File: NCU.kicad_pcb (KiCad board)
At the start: 2 copper layers, 88.5 x 126 mm, 126 parts, among them IC1 LMR51460SQDRRRQ1, IC2 TPS628101HQWRWYRQ1, J1 RJ45, J2 USB_B, J3 Micro_SD_Card, J4 6437288-4, J5 6437288-4, J6 Bus_PCI_Express_Mini, Q1 CSD25483F4, Q2 CSD25483F4, U1 STM32H745ZITx, U3 SN65HVD230, U4 SN65HVD230, U5 XL1509-3.3, U6 ESP32-C3-WROOM-02, U7 AP2112K-1.8, U8 LAN8742A

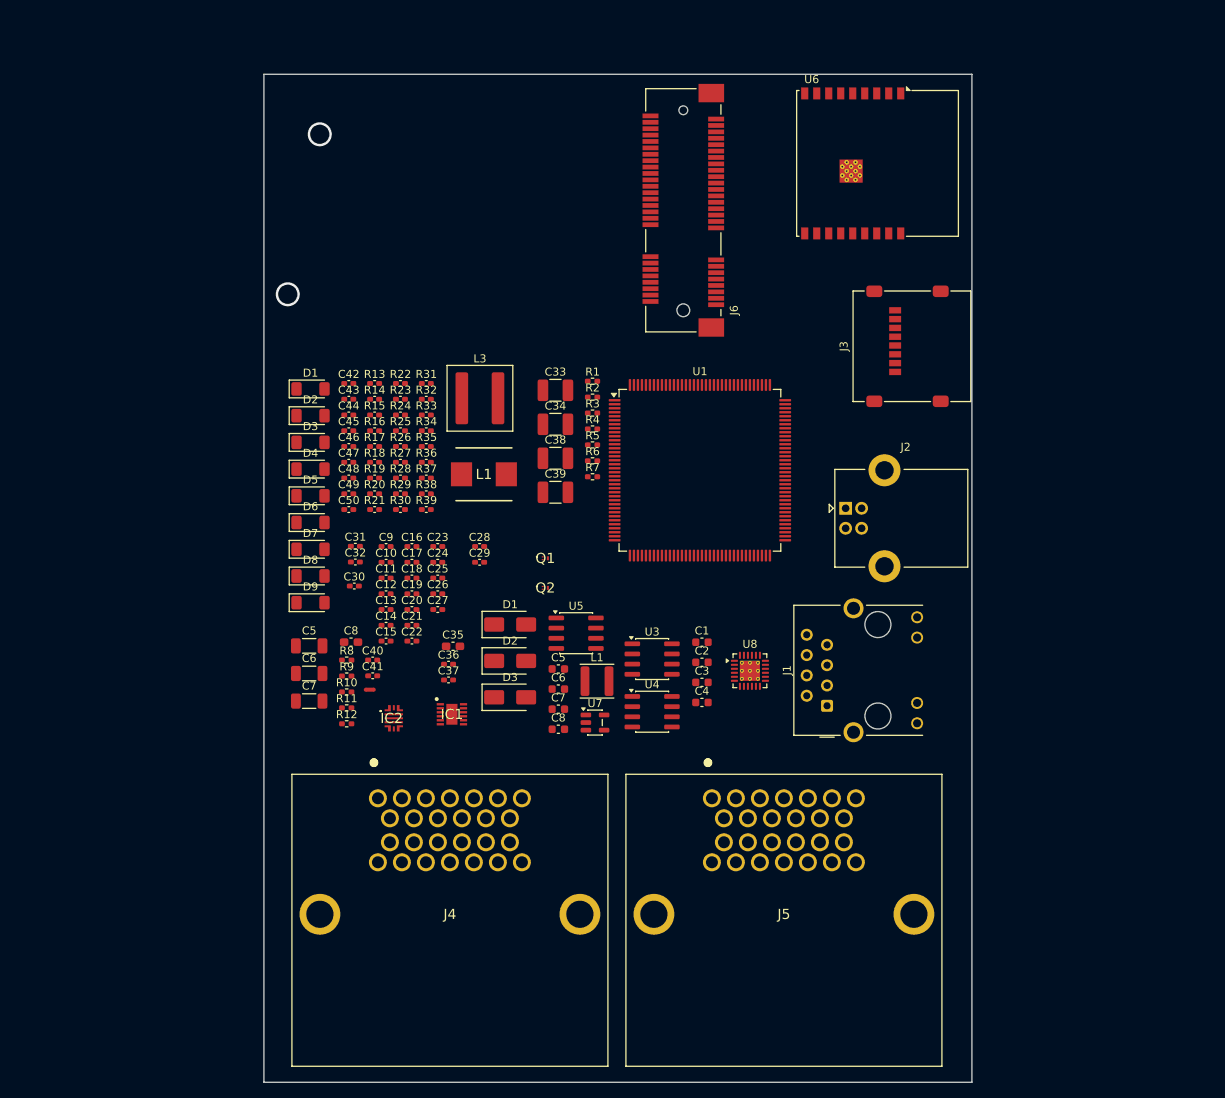
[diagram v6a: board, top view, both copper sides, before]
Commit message: redid annotations, added test point
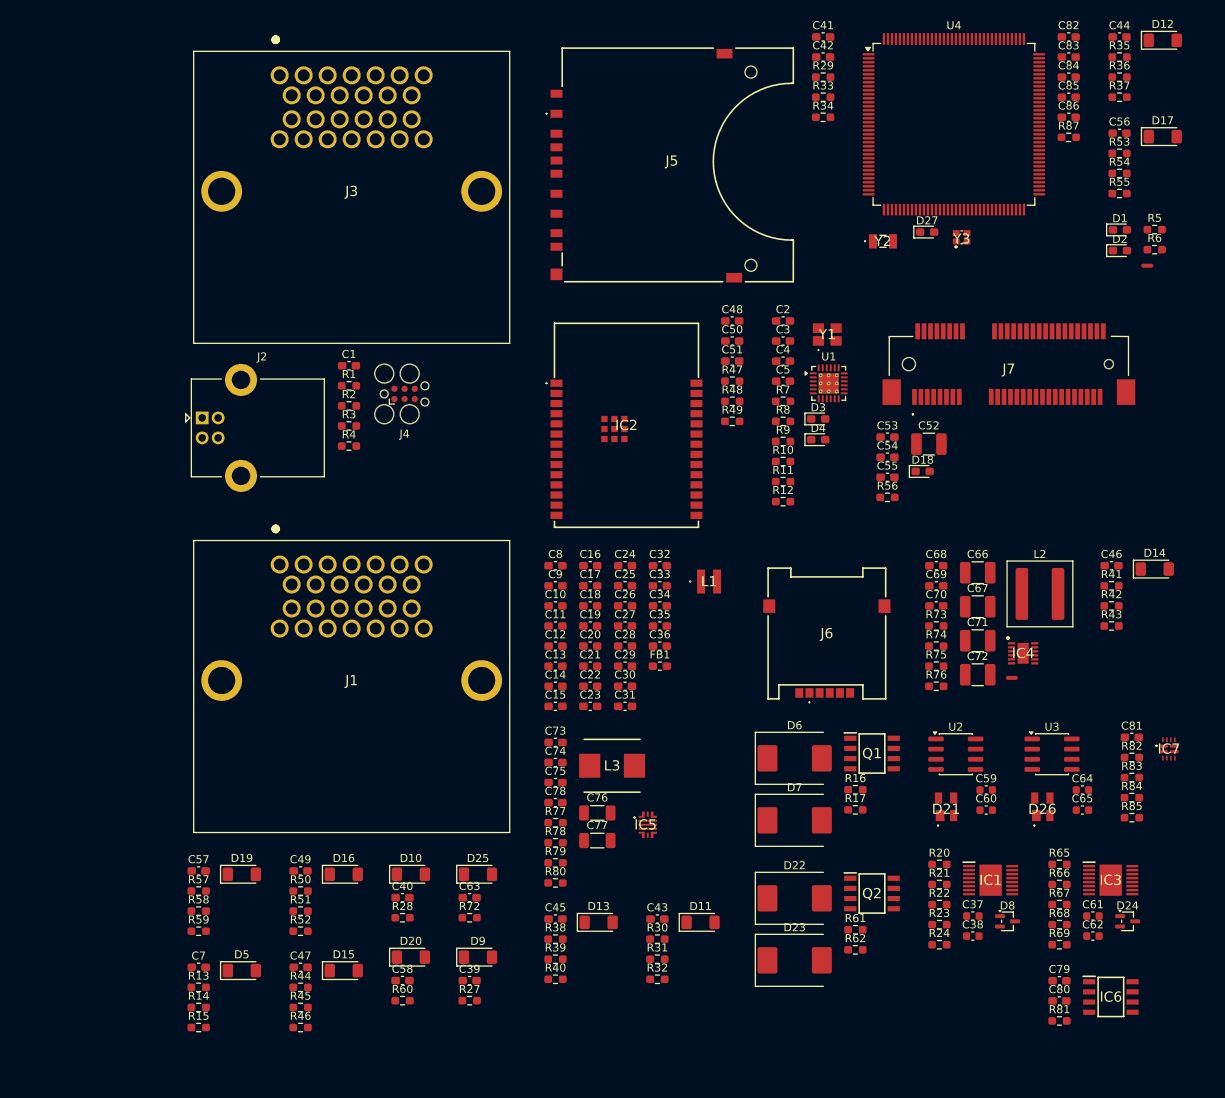
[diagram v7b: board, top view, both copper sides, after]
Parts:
- removed the C5 at (97.3, 116.8)
- removed the C5 at (66.2, 114.0)
- removed C6: 22uF, Inductor_SMD:L_1206_3216Metric_Pad1.22x1.90mm_HandSolder
- removed C6: 470uF, Capacitor_SMD:C_0603_1608Metric
- removed the C7 at (97.3, 121.9)
- removed the C7 at (66.2, 120.8)
- removed the C8 at (71.4, 113.5)
- removed the C8 at (97.3, 124.4)
- removed the D1 at (91.3, 111.3)
- removed the D1 at (66.3, 81.8)
- removed the D2 at (66.3, 85.2)
- removed the D2 at (91.3, 115.8)
- removed the D3 at (91.3, 120.4)
- removed the D3 at (66.3, 88.5)
- removed the L1 at (88.0, 92.5)
- removed the L1 at (102.2, 118.4)
- removed R18: 100, Capacitor_SMD:C_0402_1005Metric_Pad0.74x0.62mm_HandSolder
- removed R19, R25: 10k, Capacitor_SMD:C_0402_1005Metric_Pad0.74x0.62mm_HandSolder
- removed R26: 20k, Capacitor_SMD:C_0402_1005Metric_Pad0.74x0.62mm_HandSolder
- removed U5: XL1509-3.3, Package_SO:SOIC-8_3.9x4.9mm_P1.27mm
- removed U6: ESP32-C3-WROOM-02, RF_Module:ESP32-C3-WROOM-02
- removed U7: AP2112K-1.8, Package_TO_SOT_SMD:SOT-23-5
- removed U8: LAN8742A, Package_DFN_QFN:VQFN-24-1EP_4x4mm_P0.5mm_EP2.5x2.5mm_ThermalVias
- added C5: 10pF, Capacitor_SMD:C_0603_1608Metric_Pad1.08x0.95mm_HandSolder, F.Cu at (125.4, 80.9)
- added C51: 100n, Capacitor_SMD:C_0603_1608Metric_Pad1.08x0.95mm_HandSolder, F.Cu at (119.1, 78.4)
- added C52: 100uF, Capacitor_SMD:C_1210_3225Metric_Pad1.33x2.70mm_HandSolder, F.Cu at (143.6, 88.7)
- added C53: 10uF, Capacitor_SMD:C_0603_1608Metric_Pad1.08x0.95mm_HandSolder, F.Cu at (138.5, 87.9)
- added C54: 100nF, Capacitor_SMD:C_0603_1608Metric_Pad1.08x0.95mm_HandSolder, F.Cu at (138.5, 90.4)
- added C55: 100nF, Capacitor_SMD:C_0603_1608Metric_Pad1.08x0.95mm_HandSolder, F.Cu at (138.5, 92.9)
- added C56: 100nF, Capacitor_SMD:C_0603_1608Metric_Pad1.08x0.95mm_HandSolder, F.Cu at (167.5, 49.9)
- added C57: 100nF, Capacitor_SMD:C_0603_1608Metric_Pad1.08x0.95mm_HandSolder, F.Cu at (52.4, 142.1)
- added C58: 100nF, Capacitor_SMD:C_0603_1608Metric_Pad1.08x0.95mm_HandSolder, F.Cu at (77.8, 155.8)
- added C59: 1u, Capacitor_SMD:C_0603_1608Metric, F.Cu at (150.8, 132.0)
- added C60: 100n, Capacitor_SMD:C_0603_1608Metric, F.Cu at (150.8, 134.5)
- added C61: 10u, Capacitor_SMD:C_0603_1608Metric, F.Cu at (164.1, 147.7)
- added C62: 100n, Capacitor_SMD:C_0603_1608Metric, F.Cu at (164.1, 150.2)
- added C63: 100nF, Capacitor_SMD:C_0603_1608Metric_Pad1.08x0.95mm_HandSolder, F.Cu at (86.2, 145.4)
- added C64: 1u, Capacitor_SMD:C_0603_1608Metric, F.Cu at (162.8, 132.0)
- added C65: 100n, Capacitor_SMD:C_0603_1608Metric, F.Cu at (162.8, 134.5)
- added C66: 4.7uF, Capacitor_SMD:C_1210_3225Metric_Pad1.33x2.70mm_HandSolder, F.Cu at (149.7, 104.8)
- added C67: 4.7uF, Capacitor_SMD:C_1210_3225Metric_Pad1.33x2.70mm_HandSolder, F.Cu at (149.7, 109.1)
- added C68: 0.1uF, Capacitor_SMD:C_0603_1608Metric_Pad1.08x0.95mm_HandSolder, F.Cu at (144.6, 103.9)
- added C69: 0.1uF, Capacitor_SMD:C_0603_1608Metric_Pad1.08x0.95mm_HandSolder, F.Cu at (144.6, 106.4)
- added C7: 100nF, Capacitor_SMD:C_0603_1608Metric_Pad1.08x0.95mm_HandSolder, F.Cu at (52.4, 154.1)
- added C70: 33pF, Capacitor_SMD:C_0603_1608Metric_Pad1.08x0.95mm_HandSolder, F.Cu at (144.6, 109.0)
- added C71: 47uF, Capacitor_SMD:C_1210_3225Metric_Pad1.33x2.70mm_HandSolder, F.Cu at (149.7, 113.3)
- added C72: 47uF, Capacitor_SMD:C_1210_3225Metric_Pad1.33x2.70mm_HandSolder, F.Cu at (149.7, 117.6)
- added C73: 4.7nF, Capacitor_SMD:C_0603_1608Metric_Pad1.08x0.95mm_HandSolder, F.Cu at (97.0, 126.0)
- added C74: 22uF, Capacitor_SMD:C_0603_1608Metric_Pad1.08x0.95mm_HandSolder, F.Cu at (97.0, 128.5)
- added C75: 10pF, Capacitor_SMD:C_0603_1608Metric_Pad1.08x0.95mm_HandSolder, F.Cu at (97.0, 131.0)
- added C76: 22uF, Inductor_SMD:L_1206_3216Metric_Pad1.22x1.90mm_HandSolder, F.Cu at (102.2, 134.8)
- added C77: 22uF, Inductor_SMD:L_1206_3216Metric_Pad1.22x1.90mm_HandSolder, F.Cu at (102.2, 138.3)
- added C78: 22uF, Capacitor_SMD:C_0603_1608Metric_Pad1.08x0.95mm_HandSolder, F.Cu at (97.0, 133.5)
- added C79: 1uF, Capacitor_SMD:C_0603_1608Metric_Pad1.08x0.95mm_HandSolder, F.Cu at (160.0, 155.8)
- added C8: 4.7uF, Capacitor_SMD:C_0603_1608Metric_Pad1.08x0.95mm_HandSolder, F.Cu at (97.0, 103.9)
- added C80: 1uF, Capacitor_SMD:C_0603_1608Metric_Pad1.08x0.95mm_HandSolder, F.Cu at (160.0, 158.3)
- added C81: 1u, Capacitor_SMD:C_0603_1608Metric_Pad1.08x0.95mm_HandSolder, F.Cu at (169.0, 125.4)
- added C82: 100nF, Capacitor_SMD:C_0603_1608Metric_Pad1.08x0.95mm_HandSolder, F.Cu at (161.1, 37.8)
- added C83: 5.6pF, Capacitor_SMD:C_0603_1608Metric_Pad1.08x0.95mm_HandSolder, F.Cu at (161.1, 40.3)
- added C84: 5.1pF, Capacitor_SMD:C_0603_1608Metric_Pad1.08x0.95mm_HandSolder, F.Cu at (161.1, 42.9)
- added C85: 5.6pF, Capacitor_SMD:C_0603_1608Metric_Pad1.08x0.95mm_HandSolder, F.Cu at (161.1, 45.4)
- added C86: 5.1pF, Capacitor_SMD:C_0603_1608Metric_Pad1.08x0.95mm_HandSolder, F.Cu at (161.1, 47.9)
- added D1: LED, LED_SMD:LED_0603_1608Metric_Pad1.05x0.95mm_HandSolder, F.Cu at (167.5, 62.0)
- added D10: BZV55C3V6, Diode_SMD:D_MiniMELF, F.Cu at (78.9, 142.5)
- added D11: BZV55C3V6, Diode_SMD:D_MiniMELF, F.Cu at (115.1, 148.5)
- added D12: BZV55C3V6, Diode_SMD:D_MiniMELF, F.Cu at (172.9, 38.2)
- added D13: BZV55C3V6, Diode_SMD:D_MiniMELF, F.Cu at (102.4, 148.5)
- added D14: BZV55C3V6, Diode_SMD:D_MiniMELF, F.Cu at (171.9, 104.3)
- added D15: BZV55C3V6, Diode_SMD:D_MiniMELF, F.Cu at (70.5, 154.5)
- added D16: BZV55C3V6, Diode_SMD:D_MiniMELF, F.Cu at (70.5, 142.5)
- added D17: BZV55C3V6, Diode_SMD:D_MiniMELF, F.Cu at (172.9, 50.3)
- added D18: LED, LED_SMD:LED_0603_1608Metric_Pad1.05x0.95mm_HandSolder, F.Cu at (142.9, 92.1)
- added D19: BZV55C3V6, Diode_SMD:D_MiniMELF, F.Cu at (57.8, 142.5)
- added D2: LED, LED_SMD:LED_0603_1608Metric_Pad1.05x0.95mm_HandSolder, F.Cu at (167.5, 64.5)
- added D20: BZV55C3V6, Diode_SMD:D_MiniMELF, F.Cu at (78.9, 152.9)
- added D21: SP0503BAHTG, SamacSys_Parts:SP0503BAHTG, F.Cu at (145.8, 134.1)
- added D22: B340, Diode_SMD:D_SMC, F.Cu at (126.9, 145.5)
- added D23: B340, Diode_SMD:D_SMC, F.Cu at (126.9, 153.3)
- added D24: BAT54W, Package_TO_SOT_SMD:SOT-323_SC-70, F.Cu at (168.5, 148.4)
- added D25: BZV55C3V6, Diode_SMD:D_MiniMELF, F.Cu at (87.3, 142.5)
- added D26: SP0503BAHTG, SamacSys_Parts:SP0503BAHTG, F.Cu at (157.8, 134.1)
- added D27: LED, LED_SMD:LED_0603_1608Metric_Pad1.05x0.95mm_HandSolder, F.Cu at (143.4, 62.2)
- added D3: LED, LED_SMD:LED_0603_1608Metric_Pad1.05x0.95mm_HandSolder, F.Cu at (129.8, 85.6)
- added FB1: FCM 1608KF-471T03, Inductor_SMD:L_0603_1608Metric_Pad1.05x0.95mm_HandSolder, F.Cu at (110.0, 116.5)
- added IC3: VND7E025AJTR, SamacSys_Parts:SOP50P600X170-17N, F.Cu at (166.4, 143.2)
- added IC4: LMR51460SQDRRRQ1, SamacSys_Parts:SON50P300X300X80-13N-D, F.Cu at (155.4, 114.9)
- added IC5: TPS628101HQWRWYRQ1, SamacSys_Parts:TPS6281008QWRWYRQ1, F.Cu at (108.5, 136.3)
- added IC6: LP2951-50DRG4, SamacSys_Parts:SOIC127P600X175-8N, F.Cu at (166.4, 157.8)
- added IC7: TPS2121RUXT, SamacSys_Parts:TPS2121RUXT, F.Cu at (173.6, 126.8)
- added J7: 2041262-1, SamacSys_Parts:20412621, F.Cu at (141.8, 82.8)
- added L1: VLS3015CX-2R2M-H, SamacSys_Parts:VLS3015, F.Cu at (116.2, 105.9)
- added L2: 4.7uH, Inductor_SMD:L_Coilcraft_XAL7030-472, F.Cu at (157.5, 107.5)
- added NT2: NetTie_2, NetTie:NetTie-2_SMD_Pad0.5mm, F.Cu at (154.0, 118.0)
- added R40: 1.5k, Resistor_SMD:R_0603_1608Metric_Pad0.98x0.95mm_HandSolder, F.Cu at (97.0, 155.6)
- added R41: 100, Resistor_SMD:R_0603_1608Metric_Pad0.98x0.95mm_HandSolder, F.Cu at (166.5, 106.4)
- added R42: 10k, Resistor_SMD:R_0603_1608Metric_Pad0.98x0.95mm_HandSolder, F.Cu at (166.5, 109.0)
- added R43: 1k, Resistor_SMD:R_0603_1608Metric_Pad0.98x0.95mm_HandSolder, F.Cu at (166.5, 111.5)
- added R44: 100, Resistor_SMD:R_0603_1608Metric_Pad0.98x0.95mm_HandSolder, F.Cu at (65.1, 156.6)
- added R45: 10k, Resistor_SMD:R_0603_1608Metric_Pad0.98x0.95mm_HandSolder, F.Cu at (65.1, 159.1)
- added R46: 1k, Resistor_SMD:R_0603_1608Metric_Pad0.98x0.95mm_HandSolder, F.Cu at (65.1, 161.7)
- added R47: 100k, Resistor_SMD:R_0603_1608Metric_Pad0.98x0.95mm_HandSolder, F.Cu at (119.1, 80.9)
- added R48: 10k, Resistor_SMD:R_0603_1608Metric_Pad0.98x0.95mm_HandSolder, F.Cu at (119.1, 83.4)
- added R49: 10k, Resistor_SMD:R_0603_1608Metric_Pad0.98x0.95mm_HandSolder, F.Cu at (119.1, 85.9)
- added R50: 100, Resistor_SMD:R_0603_1608Metric_Pad0.98x0.95mm_HandSolder, F.Cu at (65.1, 144.6)
- added R51: 10k, Resistor_SMD:R_0603_1608Metric_Pad0.98x0.95mm_HandSolder, F.Cu at (65.1, 147.1)
- added R52: 1k, Resistor_SMD:R_0603_1608Metric_Pad0.98x0.95mm_HandSolder, F.Cu at (65.1, 149.6)
- added R53: 100, Resistor_SMD:R_0603_1608Metric_Pad0.98x0.95mm_HandSolder, F.Cu at (167.5, 52.4)
- added R54: 10k, Resistor_SMD:R_0603_1608Metric_Pad0.98x0.95mm_HandSolder, F.Cu at (167.5, 54.9)
- added R55: 1k, Resistor_SMD:R_0603_1608Metric_Pad0.98x0.95mm_HandSolder, F.Cu at (167.5, 57.4)
- added R56: 680R, Resistor_SMD:R_0603_1608Metric_Pad0.98x0.95mm_HandSolder, F.Cu at (138.5, 95.4)
- added R57: 100, Resistor_SMD:R_0603_1608Metric_Pad0.98x0.95mm_HandSolder, F.Cu at (52.4, 144.6)
- added R58: 10k, Resistor_SMD:R_0603_1608Metric_Pad0.98x0.95mm_HandSolder, F.Cu at (52.4, 147.1)
- added R59: 1k, Resistor_SMD:R_0603_1608Metric_Pad0.98x0.95mm_HandSolder, F.Cu at (52.4, 149.6)
- added R60: 100, Resistor_SMD:R_0603_1608Metric_Pad0.98x0.95mm_HandSolder, F.Cu at (77.8, 158.3)
- added R61: 33R, Resistor_SMD:R_0603_1608Metric_Pad0.98x0.95mm_HandSolder, F.Cu at (134.5, 149.4)
- added R62: 33R, Resistor_SMD:R_0603_1608Metric_Pad0.98x0.95mm_HandSolder, F.Cu at (134.5, 151.9)
- added R65: 15k, Resistor_SMD:R_0603_1608Metric_Pad0.98x0.95mm_HandSolder, F.Cu at (160.0, 141.3)
- added R66: 15k, Resistor_SMD:R_0603_1608Metric_Pad0.98x0.95mm_HandSolder, F.Cu at (160.0, 143.8)
- added R67: 15k, Resistor_SMD:R_0603_1608Metric_Pad0.98x0.95mm_HandSolder, F.Cu at (160.0, 146.3)
- added R68: 15k, Resistor_SMD:R_0603_1608Metric_Pad0.98x0.95mm_HandSolder, F.Cu at (160.0, 148.8)
- added R69: 620R, Resistor_SMD:R_0603_1608Metric_Pad0.98x0.95mm_HandSolder, F.Cu at (160.0, 151.3)
- added R72: 100, Resistor_SMD:R_0603_1608Metric_Pad0.98x0.95mm_HandSolder, F.Cu at (86.2, 147.9)
- added R73: 19.1k, Resistor_SMD:R_0603_1608Metric_Pad0.98x0.95mm_HandSolder, F.Cu at (144.6, 111.5)
- added R74: 100k, Resistor_SMD:R_0603_1608Metric_Pad0.98x0.95mm_HandSolder, F.Cu at (144.6, 114.0)
- added R75: 100k, Resistor_SMD:R_0603_1608Metric_Pad0.98x0.95mm_HandSolder, F.Cu at (144.6, 116.5)
- added R76: 1k, Resistor_SMD:R_0603_1608Metric_Pad0.98x0.95mm_HandSolder, F.Cu at (144.6, 119.0)
- added R77: 100k, Resistor_SMD:R_0603_1608Metric_Pad0.98x0.95mm_HandSolder, F.Cu at (97.0, 136.1)
- added R78: 8.06k, Resistor_SMD:R_0603_1608Metric_Pad0.98x0.95mm_HandSolder, F.Cu at (97.0, 138.6)
- added R79: 88.7k, Resistor_SMD:R_0603_1608Metric_Pad0.98x0.95mm_HandSolder, F.Cu at (97.0, 141.1)
- added R80: 19.6k, Resistor_SMD:R_0603_1608Metric_Pad0.98x0.95mm_HandSolder, F.Cu at (97.0, 143.6)
- added R81: 100k, Resistor_SMD:R_0603_1608Metric_Pad0.98x0.95mm_HandSolder, F.Cu at (160.0, 160.8)
- added R82: 18k, Resistor_SMD:R_0603_1608Metric_Pad0.98x0.95mm_HandSolder, F.Cu at (169.0, 127.9)
- added R83: 5k, Resistor_SMD:R_0603_1608Metric_Pad0.98x0.95mm_HandSolder, F.Cu at (169.0, 130.4)
- added R84: 18k, Resistor_SMD:R_0603_1608Metric_Pad0.98x0.95mm_HandSolder, F.Cu at (169.0, 132.9)
- added R85: 22.1k, Resistor_SMD:R_0603_1608Metric_Pad0.98x0.95mm_HandSolder, F.Cu at (169.0, 135.4)
- added R87: 260R, Resistor_SMD:R_0603_1608Metric_Pad0.98x0.95mm_HandSolder, F.Cu at (161.1, 50.4)
- added U2: SN65HVD230, Package_SO:SOIC-8_3.9x4.9mm_P1.27mm, F.Cu at (147.0, 127.5)
- added Y1: LFXTAL071758Cutt, SamacSys_Parts:LFXTAL071758Cutt, F.Cu at (130.9, 75.0)
- added Y2: NX3215SA-32.768K-STD-MUS-2, SamacSys_Parts:NX3215SA32768KSTDMUS2, F.Cu at (137.9, 63.4)
- added Y3: Crystal_GND24, SamacSys_Parts:NX2016SA32MEXS00ACS06465, F.Cu at (147.7, 62.9)
- C1: value 1u -> 100nF; footprint Capacitor_SMD:C_0603_1608Metric -> Capacitor_SMD:C_0603_1608Metric_Pad1.08x0.95mm_HandSolder
- C10, C11, C13, C14, C15, C16, C18, C20, C21, C22, C24, C26, C42, C43, C44, C45, C46, C47, C49: footprint Capacitor_SMD:C_0402_1005Metric_Pad0.74x0.62mm_HandSolder -> Capacitor_SMD:C_0603_1608Metric_Pad1.08x0.95mm_HandSolder
- C12: value 100nF -> 1uF; footprint Capacitor_SMD:C_0402_1005Metric_Pad0.74x0.62mm_HandSolder -> Capacitor_SMD:C_0603_1608Metric_Pad1.08x0.95mm_HandSolder
- C17, C19: value 100nF -> 10uF; footprint Capacitor_SMD:C_0402_1005Metric_Pad0.74x0.62mm_HandSolder -> Capacitor_SMD:C_0603_1608Metric_Pad1.08x0.95mm_HandSolder
- C2, C4: value 100n -> 100nF; footprint Capacitor_SMD:C_0603_1608Metric -> Capacitor_SMD:C_0603_1608Metric_Pad1.08x0.95mm_HandSolder
- C23, C25: value 1uF -> 100nF; footprint Capacitor_SMD:C_0402_1005Metric_Pad0.74x0.62mm_HandSolder -> Capacitor_SMD:C_0603_1608Metric_Pad1.08x0.95mm_HandSolder
- C27: value 4.7uF -> 220pF; footprint Capacitor_SMD:C_0402_1005Metric_Pad0.74x0.62mm_HandSolder -> Capacitor_SMD:C_0603_1608Metric_Pad1.08x0.95mm_HandSolder
- C28: value 2.2uF -> 1uF; footprint Capacitor_SMD:C_0402_1005Metric_Pad0.74x0.62mm_HandSolder -> Capacitor_SMD:C_0603_1608Metric_Pad1.08x0.95mm_HandSolder
- C29: value 2.2uF -> 10uF; footprint Capacitor_SMD:C_0402_1005Metric_Pad0.74x0.62mm_HandSolder -> Capacitor_SMD:C_0603_1608Metric_Pad1.08x0.95mm_HandSolder
- C3: value 1u -> 10uF; footprint Capacitor_SMD:C_0603_1608Metric -> Capacitor_SMD:C_0603_1608Metric_Pad1.08x0.95mm_HandSolder
- C30: value 100nF -> 2.2uF; footprint Capacitor_SMD:C_0402_1005Metric_Pad0.74x0.62mm_HandSolder -> Capacitor_SMD:C_0603_1608Metric_Pad1.08x0.95mm_HandSolder
- C31: value 220pF -> 100nF; footprint Capacitor_SMD:C_0402_1005Metric_Pad0.74x0.62mm_HandSolder -> Capacitor_SMD:C_0603_1608Metric_Pad1.08x0.95mm_HandSolder
- C32: value 10uF -> 2.2uF; footprint Capacitor_SMD:C_0402_1005Metric_Pad0.74x0.62mm_HandSolder -> Capacitor_SMD:C_0603_1608Metric_Pad1.08x0.95mm_HandSolder
- C33: value 4.7uF -> 100nF; footprint Capacitor_SMD:C_1210_3225Metric_Pad1.33x2.70mm_HandSolder -> Capacitor_SMD:C_0603_1608Metric_Pad1.08x0.95mm_HandSolder
- C34: value 4.7uF -> 1uF; footprint Capacitor_SMD:C_1210_3225Metric_Pad1.33x2.70mm_HandSolder -> Capacitor_SMD:C_0603_1608Metric_Pad1.08x0.95mm_HandSolder
- C35: value 0.1uF -> 100nF
- C36: value 0.1uF -> 100nF; footprint Capacitor_SMD:C_0402_1005Metric_Pad0.74x0.62mm_HandSolder -> Capacitor_SMD:C_0603_1608Metric_Pad1.08x0.95mm_HandSolder
- C37: value 33pF -> 10u; footprint Capacitor_SMD:C_0402_1005Metric_Pad0.74x0.62mm_HandSolder -> Capacitor_SMD:C_0603_1608Metric
- C38: value 47uF -> 100n; footprint Capacitor_SMD:C_1210_3225Metric_Pad1.33x2.70mm_HandSolder -> Capacitor_SMD:C_0603_1608Metric
- C39: value 47uF -> 100nF; footprint Capacitor_SMD:C_1210_3225Metric_Pad1.33x2.70mm_HandSolder -> Capacitor_SMD:C_0603_1608Metric_Pad1.08x0.95mm_HandSolder
- C40: value 4.7nF -> 100nF; footprint Capacitor_SMD:C_0402_1005Metric_Pad0.74x0.62mm_HandSolder -> Capacitor_SMD:C_0603_1608Metric_Pad1.08x0.95mm_HandSolder
- C41: value 10pF -> 10uF; footprint Capacitor_SMD:C_0402_1005Metric_Pad0.74x0.62mm_HandSolder -> Capacitor_SMD:C_0603_1608Metric_Pad1.08x0.95mm_HandSolder
- C48: value 100nF -> 1u; footprint Capacitor_SMD:C_0402_1005Metric_Pad0.74x0.62mm_HandSolder -> Capacitor_SMD:C_0603_1608Metric_Pad1.08x0.95mm_HandSolder
- C50: value 100nF -> 10u; footprint Capacitor_SMD:C_0402_1005Metric_Pad0.74x0.62mm_HandSolder -> Capacitor_SMD:C_0603_1608Metric_Pad1.08x0.95mm_HandSolder
- C9: value 4.7uF -> 100nF; footprint Capacitor_SMD:C_0402_1005Metric_Pad0.74x0.62mm_HandSolder -> Capacitor_SMD:C_0603_1608Metric_Pad1.08x0.95mm_HandSolder
- D4: value BZV55C3V6 -> LED; footprint Diode_SMD:D_MiniMELF -> LED_SMD:LED_0603_1608Metric_Pad1.05x0.95mm_HandSolder
- D6, D7: value BZV55C3V6 -> B340; footprint Diode_SMD:D_MiniMELF -> Diode_SMD:D_SMC
- D8: value BZV55C3V6 -> BAT54W; footprint Diode_SMD:D_MiniMELF -> Package_TO_SOT_SMD:SOT-323_SC-70
- IC1: value LMR51460SQDRRRQ1 -> VND7E025AJTR; footprint SamacSys_Parts:SON50P300X300X80-13N-D -> SamacSys_Parts:SOP50P600X170-17N
- IC2: value TPS628101HQWRWYRQ1 -> ESP32-C6-WROOM-1-N8; footprint SamacSys_Parts:TPS6281008QWRWYRQ1 -> SamacSys_Parts:ESP32C6WROOM1N8
- J1: value RJ45 -> 6437288-4; footprint Connector_RJ:RJ45_Hanrun_HR911105A_Horizontal -> SamacSys_Parts:64372884
- J3: value Micro_SD_Card -> 6437288-4; footprint Connector_Card:microSD_HC_Molex_47219-2001 -> SamacSys_Parts:64372884
- J4: value 6437288-4 -> Conn_ARM_SWD_TagConnect_TC2030; footprint SamacSys_Parts:64372884 -> Connector:Tag-Connect_TC2030-IDC-FP_2x03_P1.27mm_Vertical
- J5: value 6437288-4 -> GSD09002SEU; footprint SamacSys_Parts:64372884 -> SamacSys_Parts:GSD09002SEU
- J6: value Bus_PCI_Express_Mini -> MSIM-11-C; footprint Connector_PCBEdge:BUS_PCI_Express_Mini_Full -> SamacSys_Parts:MSIM11C
- L3: value 4.7uH -> 0.47uH; footprint Inductor_SMD:L_Coilcraft_XAL7030-472 -> SamacSys_Parts:INDPM7066X240N
- Q1, Q2: value CSD25483F4 -> STS5DNF60L; footprint SamacSys_Parts:CSD25483F4T -> SamacSys_Parts:SOIC127P600X175-8N
- R1, R4: value 100k -> 47R; footprint Resistor_SMD:R_0402_1005Metric_Pad0.72x0.64mm_HandSolder -> Resistor_SMD:R_0603_1608Metric_Pad0.98x0.95mm_HandSolder
- R10: value 19.6k -> 12.4k; footprint Resistor_SMD:R_0402_1005Metric_Pad0.72x0.64mm_HandSolder -> Resistor_SMD:R_0603_1608Metric_Pad0.98x0.95mm_HandSolder
- R11, R12: value 100k -> 10k; footprint Resistor_SMD:R_0402_1005Metric_Pad0.72x0.64mm_HandSolder -> Resistor_SMD:R_0603_1608Metric_Pad0.98x0.95mm_HandSolder
- R13, R27, R30, R34: footprint Capacitor_SMD:C_0402_1005Metric_Pad0.74x0.62mm_HandSolder -> Resistor_SMD:R_0603_1608Metric_Pad0.98x0.95mm_HandSolder
- R14, R31: value 10k -> 1k; footprint Capacitor_SMD:C_0402_1005Metric_Pad0.74x0.62mm_HandSolder -> Resistor_SMD:R_0603_1608Metric_Pad0.98x0.95mm_HandSolder
- R15, R32: value 20k -> 1.5k; footprint Capacitor_SMD:C_0402_1005Metric_Pad0.74x0.62mm_HandSolder -> Resistor_SMD:R_0603_1608Metric_Pad0.98x0.95mm_HandSolder
- R16: value 10k -> 33R; footprint Capacitor_SMD:C_0402_1005Metric_Pad0.74x0.62mm_HandSolder -> Resistor_SMD:R_0603_1608Metric_Pad0.98x0.95mm_HandSolder
- R17: value 20k -> 33R; footprint Capacitor_SMD:C_0402_1005Metric_Pad0.74x0.62mm_HandSolder -> Resistor_SMD:R_0603_1608Metric_Pad0.98x0.95mm_HandSolder
- R2: value 19.1k -> 47R; footprint Resistor_SMD:R_0402_1005Metric_Pad0.72x0.64mm_HandSolder -> Resistor_SMD:R_0603_1608Metric_Pad0.98x0.95mm_HandSolder
- R20, R23: value 20k -> 15k; footprint Capacitor_SMD:C_0402_1005Metric_Pad0.74x0.62mm_HandSolder -> Resistor_SMD:R_0603_1608Metric_Pad0.98x0.95mm_HandSolder
- R21: value 100 -> 15k; footprint Capacitor_SMD:C_0402_1005Metric_Pad0.74x0.62mm_HandSolder -> Resistor_SMD:R_0603_1608Metric_Pad0.98x0.95mm_HandSolder
- R22: value 10k -> 15k; footprint Capacitor_SMD:C_0402_1005Metric_Pad0.74x0.62mm_HandSolder -> Resistor_SMD:R_0603_1608Metric_Pad0.98x0.95mm_HandSolder
- R24: value 100 -> 620R; footprint Capacitor_SMD:C_0402_1005Metric_Pad0.74x0.62mm_HandSolder -> Resistor_SMD:R_0603_1608Metric_Pad0.98x0.95mm_HandSolder
- R28: value 10k -> 100; footprint Capacitor_SMD:C_0402_1005Metric_Pad0.74x0.62mm_HandSolder -> Resistor_SMD:R_0603_1608Metric_Pad0.98x0.95mm_HandSolder
- R29: value 20k -> 10R; footprint Capacitor_SMD:C_0402_1005Metric_Pad0.74x0.62mm_HandSolder -> Resistor_SMD:R_0603_1608Metric_Pad0.98x0.95mm_HandSolder
- R3: value 1k -> 47R; footprint Resistor_SMD:R_0402_1005Metric_Pad0.72x0.64mm_HandSolder -> Resistor_SMD:R_0603_1608Metric_Pad0.98x0.95mm_HandSolder
- R33: value 100 -> 10k; footprint Capacitor_SMD:C_0402_1005Metric_Pad0.74x0.62mm_HandSolder -> Resistor_SMD:R_0603_1608Metric_Pad0.98x0.95mm_HandSolder
- R35, R38: value 20k -> 100; footprint Capacitor_SMD:C_0402_1005Metric_Pad0.74x0.62mm_HandSolder -> Resistor_SMD:R_0603_1608Metric_Pad0.98x0.95mm_HandSolder
- R36, R39: value 100 -> 1k; footprint Capacitor_SMD:C_0402_1005Metric_Pad0.74x0.62mm_HandSolder -> Resistor_SMD:R_0603_1608Metric_Pad0.98x0.95mm_HandSolder
- R37: value 10k -> 1.5k; footprint Capacitor_SMD:C_0402_1005Metric_Pad0.74x0.62mm_HandSolder -> Resistor_SMD:R_0603_1608Metric_Pad0.98x0.95mm_HandSolder
- R5: value 10k -> 2k; footprint Resistor_SMD:R_0402_1005Metric_Pad0.72x0.64mm_HandSolder -> Resistor_SMD:R_0603_1608Metric_Pad0.98x0.95mm_HandSolder
- R6: value 100k -> 260R; footprint Resistor_SMD:R_0402_1005Metric_Pad0.72x0.64mm_HandSolder -> Resistor_SMD:R_0603_1608Metric_Pad0.98x0.95mm_HandSolder
- R7: value 10k -> 680R; footprint Resistor_SMD:R_0402_1005Metric_Pad0.72x0.64mm_HandSolder -> Resistor_SMD:R_0603_1608Metric_Pad0.98x0.95mm_HandSolder
- R8: value 8.06k -> 10R; footprint Resistor_SMD:R_0402_1005Metric_Pad0.72x0.64mm_HandSolder -> Resistor_SMD:R_0603_1608Metric_Pad0.98x0.95mm_HandSolder
- R9: value 88.7k -> 680R; footprint Resistor_SMD:R_0402_1005Metric_Pad0.72x0.64mm_HandSolder -> Resistor_SMD:R_0603_1608Metric_Pad0.98x0.95mm_HandSolder
- U1: value STM32H745ZITx -> LAN8742A; footprint Package_QFP:LQFP-144_20x20mm_P0.5mm -> Package_DFN_QFN:VQFN-24-1EP_4x4mm_P0.5mm_EP2.5x2.5mm_ThermalVias
- U4: value SN65HVD230 -> STM32H745ZITx; footprint Package_SO:SOIC-8_3.9x4.9mm_P1.27mm -> Package_QFP:LQFP-144_20x20mm_P0.5mm
- moved NT1 110.7 mm to (170.9, 66.4)
- moved C44 107.3 mm to (167.5, 37.8)
- moved R35 99.4 mm to (167.5, 40.3)
- moved R36 99.1 mm to (167.5, 42.9)
- moved R37 98.9 mm to (167.5, 45.4)
- moved C41 97.7 mm to (130.4, 37.8)
- moved D8 97.2 mm to (153.5, 148.4)
- moved C46 96.5 mm to (166.5, 103.9)
- moved R24 94.5 mm to (145.0, 151.3)
- moved R23 94.1 mm to (145.0, 148.8)
- moved R22 93.7 mm to (145.0, 146.3)
- moved J3 86.0 mm to (62.5, 42.6), turned to 0 degrees
- moved R21 84.7 mm to (145.0, 143.8)
- moved R20 84.4 mm to (145.0, 141.3)
- moved U4 82.6 mm to (146.8, 48.8)
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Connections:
- C1 pad 1: +3V3 -> 3V3
- C10 pad 1: +3V3 -> 3V3
- C11 pad 1: +3V3 -> 3V3
- C12 pad 1: +3V3 -> 3V3
- C13 pad 1: +3V3 -> 3V3
- C14 pad 1: +3V3 -> 3V3
- C15 pad 1: +3V3 -> 3V3
- C16 pad 1: +3V3 -> 3V3
- C17 pad 1: +3V3 -> 3V3
- C18 pad 1: +3V3 -> 3V3
- C19 pad 1: +3V3 -> 3V3
- C2 pad 1: +3V3 -> Net-(U1-VDD1A)
- C20 pad 1: +3V3 -> 3V3
- C21 pad 1: +3V3 -> 3V3
- C22 pad 1: +3V3 -> 3V3
- C23 pad 1: +3V3 -> 3V3
- C24 pad 1: +3V3 -> 3V3
- C25 pad 1: +3V3 -> 3V3
- C26 pad 1: +3V3 -> 3V3
- C27 pad 1: +3V3 -> /MCU/VLXSMPS
- C28 pad 1: Net-(C28-Pad1) -> /MCU/VREF+
- C28 pad 2: GND -> AGND
- C29 pad 1: Net-(C28-Pad1) -> /MCU/MCU Power/1V2_MCU
- C3 pad 1: +3V3 -> Net-(U1-VDD1A)
- C30 pad 1: +3V3 -> /MCU/VCAP
- C31 pad 1: Net-(U1-VLXSMPS) -> /MCU/VREF+
- C31 pad 2: GND -> AGND
- C32 pad 1: Net-(U1-VFBSMPS) -> /MCU/VCAP
- C33 pad 1: +12V -> /MCU/MCU Power/1V2_MCU
- C34 pad 1: +12V -> /MCU/VREF+
- C34 pad 2: GND -> AGND
- C35 pad 1: +12V -> /MCU/MCU Power/1V2_MCU
- C36 pad 1: Net-(IC1-SW_1) -> /MCU/VREF+
- C36 pad 2: Net-(IC1-BOOT) -> AGND
- C37 pad 1: Net-(C37-Pad1) -> 12V
- C37 pad 2: /Power Supplies/LMR_FB -> GND
- C38 pad 1: CAR_5V -> 12V
- C39 pad 1: CAR_5V -> /GPIO/GPIO1_IO
- C4 pad 1: +3V3 -> 3V3
- C40 pad 1: Net-(IC2-SS/TR) -> /GPIO/GPIO2_IO
- C41 pad 1: +3V3 -> Net-(J5-MMC-VDD/SD-VDD)
- C41 pad 2: /Power Supplies/TPS_FB -> GND
- C42 pad 1: /Analog Inputs/12V_ADC -> Net-(J5-MMC-VDD/SD-VDD)
- C43 pad 1: /Analog Inputs/A0_ADC -> /INPUTS/INPUT_5V_2/IO
- C43 pad 2: GND -> AGND
- C44 pad 1: /Analog Inputs/A1_ADC -> /INPUTS/INPUT_5V_0/IO
- C44 pad 2: GND -> AGND
- C45 pad 1: /Analog Inputs/A2_ADC -> /INPUTS/INPUT_5V_3/IO
- C45 pad 2: GND -> AGND
- C46 pad 1: /Analog Inputs/A3_ADC -> /INPUTS/INPUT_20V_1/IO
- C47 pad 1: /Analog Inputs/A4_ADC -> /INPUTS/INPUT_20V_2/IO
- C48 pad 1: /Analog Inputs/A5_ADC -> /CONN_B/ESP_EN
- C49 pad 1: /Analog Inputs/A6_ADC -> /INPUTS/INPUT_20V_0/IO
- C50 pad 1: /Analog Inputs/A7_ADC -> 3V3
- C9 pad 1: +3V3 -> 3V3
- D4 pad 1: /Analog Inputs/A2_ADC -> GND
- D4 pad 2: GND -> Net-(D4-A)
- D5 pad 1: /Analog Inputs/A3_ADC -> /INPUTS/INPUT_5V_1/IO
- D5 pad 2: GND -> AGND
- D6 pad 1: /Analog Inputs/A4_ADC -> 12V
- D6 pad 2: GND -> /CONN_A/LSD_2
- D7 pad 1: /Analog Inputs/A5_ADC -> 12V
- D7 pad 2: GND -> /CONN_A/LSD_3
- D8 pad 1: /Analog Inputs/A6_ADC -> GND
- D8 pad 2: GND -> unconnected-(D8-NC-Pad2)
- D9 pad 1: /Analog Inputs/A7_ADC -> /GPIO/GPIO1_IO
- IC1 pad 1: Net-(IC1-SW_1) -> Net-(IC1-INPUT0)
- IC1 pad 10: +12V -> /CONN_A/HSD_3
- IC1 pad 11: +12V -> /CONN_A/HSD_3
- IC1 pad 12: +12V -> /CONN_A/HSD_3
- IC1 pad 13: GND -> /CONN_A/HSD_2
- IC1 pad 2: Net-(IC1-SW_1) -> Net-(IC1-~{FAULTRST})
- IC1 pad 3: Net-(IC1-SW_1) -> Net-(IC1-SEN)
- IC1 pad 4: Net-(IC1-BOOT) -> Net-(D8-K)
- IC1 pad 5: /Power Supplies/12V_PG -> Net-(IC1-SEL0)
- IC1 pad 7: /Power Supplies/LMR_FB -> /DRIVES/HSD23_ISEN
- IC1 pad 8: Net-(IC1-AGND) -> Net-(IC1-INPUT1)
- IC1 pad 9: +12V -> /CONN_A/HSD_3
- IC2 pad 1: +5V -> GND
- IC2 pad 10: +5V -> Net-(IC2-IO8)
- IC2 pad 11: /Power Supplies/TPS_FB -> unconnected-(IC2-IO10-Pad11)
- IC2 pad 12: /Power Supplies/TPS_CF -> unconnected-(IC2-IO11-Pad12)
- IC2 pad 13: +5V -> unconnected-(IC2-IO12-Pad13)
- IC2 pad 2: +5V -> 3V3
- IC2 pad 3: Net-(IC2-SW) -> /CONN_B/ESP_EN
- IC2 pad 4: GND -> unconnected-(IC2-IO4-Pad4)
- IC2 pad 5: /Power Supplies/TPS_FB -> unconnected-(IC2-IO5-Pad5)
- IC2 pad 6: Net-(IC2-SS/TR) -> /MCU/ESP_SPI_CLK
- IC2 pad 7: /Power Supplies/TPS_CF -> /MCU/ESP_SPI_MOSI
- IC2 pad 8: +5V -> unconnected-(IC2-IO0-Pad8)
- IC2 pad 9: /Power Supplies/3V3_PG -> unconnected-(IC2-IO1-Pad9)
- J1 pad 1: unconnected-(J1-Pad1) -> GND
- J1 pad 10: (no net) -> /CONN_A/LSD_1
- J1 pad 11: (no net) -> /CONN_A/LSD_2
- J1 pad 12: (no net) -> /CONN_A/LSD_3
- J1 pad 2: unconnected-(J1-Pad2) -> GND
- J1 pad 3: unconnected-(J1-Pad3) -> 12V
- J1 pad 4: unconnected-(J1-Pad4) -> 12V
- J1 pad 5: unconnected-(J1-Pad5) -> /CONN_A/CAN0_L
- J1 pad 6: unconnected-(J1-Pad6) -> /CONN_A/CAN0_H
- J1 pad 7: unconnected-(J1-Pad7) -> /CONN_A/CAN1_L
- J1 pad 8: unconnected-(J1-Pad8) -> /CONN_A/CAN1_H
- J1 pad 9: (no net) -> /CONN_A/LSD_0
- J2 pad 1: USB_5V -> USB_VBUS
- J2 pad 2: unconnected-(J2-D--Pad2) -> /CONN_B/STM_USB_DM
- J2 pad 3: unconnected-(J2-D+-Pad3) -> /CONN_B/STM_USB_DP
- J3 pad 1: unconnected-(J3-DAT2-Pad1) -> GND
- J3 pad 2: unconnected-(J3-DAT3/CD-Pad2) -> USB_VBUS
- J3 pad 3: unconnected-(J3-CMD-Pad3) -> /CONN_B/STM_USB_DP
- J3 pad 4: unconnected-(J3-VDD-Pad4) -> /CONN_B/STM_USB_DM
- J3 pad 5: unconnected-(J3-CLK-Pad5) -> /CONN_B/PCIE_USB_DP
- J3 pad 6: unconnected-(J3-VSS-Pad6) -> /CONN_B/PCIE_USB_DM
- J3 pad 7: unconnected-(J3-DAT0-Pad7) -> /CONN_B/ETH_TXP
- J3 pad 8: unconnected-(J3-DAT1-Pad8) -> /CONN_B/ETH_TXM
- J3 pad 9: unconnected-(J3-SHIELD-Pad9) -> /CONN_B/ETH_RXP
- J4 pad 1: unconnected-(J4-Pad1) -> 3V3
- J4 pad 2: unconnected-(J4-Pad2) -> Net-(J4-SWDIO)
- J4 pad 3: unconnected-(J4-Pad3) -> Net-(J4-~{RESET})
- J4 pad 4: unconnected-(J4-Pad4) -> Net-(J4-SWCLK)
- J4 pad 5: unconnected-(J4-Pad5) -> GND
- J4 pad 6: unconnected-(J4-Pad6) -> Net-(J4-SWO)
- J5 pad 1: unconnected-(J5-Pad1) -> /CARD_SD/SD_DAT3
- J5 pad 10: unconnected-(J5-Pad10) -> /CARD_SD/SD_CD
- J5 pad 11: unconnected-(J5-Pad11) -> /CARD_SD/SD_WP
- J5 pad 12: unconnected-(J5-Pad12) -> GND
- J5 pad 13: unconnected-(J5-Pad13) -> GND
- J5 pad 2: unconnected-(J5-Pad2) -> /CARD_SD/SD_CMD
- J5 pad 3: unconnected-(J5-Pad3) -> GND
- J5 pad 4: unconnected-(J5-Pad4) -> Net-(J5-MMC-VDD/SD-VDD)
- J5 pad 5: unconnected-(J5-Pad5) -> /CARD_SD/SD_CLK
- J5 pad 6: unconnected-(J5-Pad6) -> GND
- J5 pad 7: unconnected-(J5-Pad7) -> /CARD_SD/SD_DAT0
- J5 pad 8: unconnected-(J5-Pad8) -> /CARD_SD/SD_DAT1
- J5 pad 9: unconnected-(J5-Pad9) -> /CARD_SD/SD_DAT2
- L3 pad 1: Net-(IC1-SW_1) -> Net-(IC5-SW)
- L3 pad 2: CAR_5V -> 3V3
- NT1 pad 2: Net-(IC1-AGND) -> AGND
- Q1 pad 1: Net-(Q1-Pad1) -> GND
- Q1 pad 2: CAR_5V -> Net-(Q1-G1)
- Q1 pad 3: +5V -> GND
- Q2 pad 1: Net-(Q2-Pad1) -> GND
- Q2 pad 2: USB_5V -> Net-(Q2-G1)
- Q2 pad 3: +5V -> GND
- R1 pad 1: CAR_5V -> /CONN_B/STM_SWDIO
- R1 pad 2: /Power Supplies/LMR_FB -> Net-(J4-SWDIO)
- R10 pad 2: /Power Supplies/TPS_FB -> Net-(U1-RBIAS)
- R11 pad 1: /Power Supplies/12V_PG -> 3V3
- R11 pad 2: +3V3 -> /MCU/ETH_RST
- R12 pad 1: /Power Supplies/3V3_PG -> 3V3
- R12 pad 2: +3V3 -> /MCU/ETH_INT
- R13 pad 1: Net-(R13-Pad1) -> /INPUTS/INPUT_5V_1/RAW
- R13 pad 2: /Analog Inputs/12V_ADC -> Net-(R13-Pad2)
- R14 pad 1: /Analog Inputs/12V -> Net-(R13-Pad2)
- R14 pad 2: Net-(R13-Pad1) -> /INPUTS/INPUT_5V_1/IO
- R15 pad 1: Net-(R13-Pad1) -> /INPUTS/INPUT_5V_1/IO
- R15 pad 2: GND -> AGND
- R16 pad 1: /Analog Inputs/A0_RAW -> /DRIVES/LSD2_CTRL
- R16 pad 2: Net-(R16-Pad2) -> Net-(Q1-G1)
- R17 pad 1: Net-(R16-Pad2) -> /DRIVES/LSD3_CTRL
- R17 pad 2: GND -> Net-(Q1-G2)
- R2 pad 1: /Power Supplies/LMR_FB -> /CONN_B/STM_SWDCLK
- R2 pad 2: Net-(IC1-AGND) -> Net-(J4-SWCLK)
- R20 pad 1: Net-(R19-Pad2) -> /DRIVES/HSD2_CTRL
- R20 pad 2: GND -> Net-(IC1-INPUT0)
- R21 pad 1: Net-(R19-Pad2) -> /DRIVES/HSD23_EN
- R21 pad 2: /Analog Inputs/A1_ADC -> Net-(IC1-SEN)
- R22 pad 1: /Analog Inputs/A2_RAW -> /DRIVES/HSD23_SEL
- R22 pad 2: Net-(R22-Pad2) -> Net-(IC1-SEL0)
- R23 pad 1: Net-(R22-Pad2) -> /DRIVES/HSD3_CTRL
- R23 pad 2: GND -> Net-(IC1-INPUT1)
- R24 pad 1: Net-(R22-Pad2) -> GND
- R24 pad 2: /Analog Inputs/A2_ADC -> /DRIVES/HSD23_ISEN
- R27 pad 1: Net-(R25-Pad2) -> /CONN_B/GPIO_1
- R27 pad 2: /Analog Inputs/A3_ADC -> /GPIO/GPIO1_IO
- R28 pad 1: /Analog Inputs/A4_RAW -> /CONN_B/GPIO_2
- R28 pad 2: Net-(R28-Pad2) -> /GPIO/GPIO2_IO
- R29 pad 1: Net-(R28-Pad2) -> Net-(J5-MMC-VDD/SD-VDD)
- R29 pad 2: GND -> 3V3
- R3 pad 1: CAR_5V -> /CONN_B/STM_SWO
- R3 pad 2: Net-(C37-Pad1) -> Net-(J4-SWO)
- R30 pad 1: Net-(R28-Pad2) -> /INPUTS/INPUT_5V_2/RAW
- R30 pad 2: /Analog Inputs/A4_ADC -> Net-(R30-Pad2)
- R31 pad 1: /Analog Inputs/A5_RAW -> Net-(R30-Pad2)
- R31 pad 2: Net-(R31-Pad2) -> /INPUTS/INPUT_5V_2/IO
- R32 pad 1: Net-(R31-Pad2) -> /INPUTS/INPUT_5V_2/IO
- R32 pad 2: GND -> AGND
- R33 pad 1: Net-(R31-Pad2) -> 3V3
- R33 pad 2: /Analog Inputs/A5_ADC -> /CARD_SD/SD_CD
- R34 pad 1: /Analog Inputs/A6_RAW -> 3V3
- R34 pad 2: Net-(R34-Pad2) -> /CARD_SD/SD_WP
- R35 pad 1: Net-(R34-Pad2) -> /INPUTS/INPUT_5V_0/RAW
- R35 pad 2: GND -> Net-(R35-Pad2)
- R36 pad 1: Net-(R34-Pad2) -> Net-(R35-Pad2)
- R36 pad 2: /Analog Inputs/A6_ADC -> /INPUTS/INPUT_5V_0/IO
- R37 pad 1: /Analog Inputs/A7_RAW -> /INPUTS/INPUT_5V_0/IO
- R37 pad 2: Net-(R37-Pad2) -> AGND
- R38 pad 1: Net-(R37-Pad2) -> /INPUTS/INPUT_5V_3/RAW
- R38 pad 2: GND -> Net-(R38-Pad2)
- R39 pad 1: Net-(R37-Pad2) -> Net-(R38-Pad2)
- R39 pad 2: /Analog Inputs/A7_ADC -> /INPUTS/INPUT_5V_3/IO
- R4 pad 1: CAR_5V -> /CONN_B/STM_NRST
- R4 pad 2: Net-(Q1-Pad1) -> Net-(J4-~{RESET})
- R5 pad 1: Net-(Q1-Pad1) -> 12V
- R5 pad 2: +5V -> Net-(D1-A)
- R6 pad 1: USB_5V -> 3V3
- R6 pad 2: Net-(Q2-Pad1) -> Net-(D2-A)
- R7 pad 1: Net-(Q2-Pad1) -> 3V3
- R7 pad 2: +5V -> Net-(D3-K)
- R8 pad 1: GND -> 3V3
- R8 pad 2: /Power Supplies/TPS_CF -> Net-(U1-VDD1A)
- R9 pad 1: /Power Supplies/TPS_FB -> Net-(U1-LED1/REGOFF)
- R9 pad 2: +3V3 -> Net-(D4-A)
- U1 pad 1: unconnected-(U1-PE2-Pad1) -> Net-(U1-VDD1A)
- U1 pad 10: unconnected-(U1-PC14-Pad10) -> GND
- U1 pad 11: unconnected-(U1-PC15-Pad11) -> /MCU/ETH_CRS_DV
- U1 pad 12: GND -> /MCU/ETH_MDIO
- U1 pad 13: +3V3 -> /MCU/ETH_MDC
- U1 pad 14: GND -> /MCU/ETH_INT
- U1 pad 15: Net-(U1-VLXSMPS) -> /MCU/ETH_RST
- U1 pad 16: +3V3 -> /MCU/ETH_TXEN
- U1 pad 17: Net-(U1-VFBSMPS) -> /MCU/ETH_TXD0
- U1 pad 18: GND -> /MCU/ETH_TXD1
- U1 pad 19: +3V3 -> Net-(U1-VDD1A)
- U1 pad 2: unconnected-(U1-PE3-Pad2) -> Net-(D3-A)
- U1 pad 20: unconnected-(U1-PF6-Pad20) -> /CONN_B/ETH_TXM
- U1 pad 21: unconnected-(U1-PF7-Pad21) -> /CONN_B/ETH_TXP
- U1 pad 22: unconnected-(U1-PF8-Pad22) -> /CONN_B/ETH_RXM
- U1 pad 23: unconnected-(U1-PF9-Pad23) -> /CONN_B/ETH_RXP
- U1 pad 24: unconnected-(U1-PF10-Pad24) -> Net-(U1-RBIAS)
- U1 pad 25: unconnected-(U1-PH0-Pad25) -> GND
- U1 pad 3: unconnected-(U1-PE4-Pad3) -> Net-(U1-LED1/REGOFF)
- U1 pad 4: unconnected-(U1-PE5-Pad4) -> Net-(U1-XTAL2)
- U1 pad 5: unconnected-(U1-PE6-Pad5) -> Net-(U1-XTAL1/CLKIN)
- U1 pad 6: GND -> 3V3
- U1 pad 7: +3V3 -> /MCU/ETH_RXD1
- U1 pad 8: +3V3 -> /MCU/ETH_RXD0
- U1 pad 9: unconnected-(U1-PC13-Pad9) -> 3V3
- U3 pad 1: /MCU/FDCAN1_TX -> /MCU/CAN0_TX
- U3 pad 3: +3V3 -> 3V3
- U3 pad 4: /MCU/FDCAN1_RX -> /MCU/CAN0_RX
- U3 pad 6: /CAN/CAN0_LO -> /CONN_A/CAN0_L
- U3 pad 7: /CAN/CAN0_HI -> /CONN_A/CAN0_H
- U4 pad 1: /MCU/FDCAN2_TX -> /MCU/ESP_SPI_CLK
- U4 pad 2: GND -> unconnected-(U4-PE3-Pad2)
- U4 pad 3: +3V3 -> /MCU/ESP_SPI_CS
- U4 pad 4: /MCU/FDCAN2_RX -> /MCU/ESP_SPI_MISO
- U4 pad 5: unconnected-(U4-Vref-Pad5) -> /MCU/ESP_SPI_MOSI
- U4 pad 6: /CAN/CAN1_LO -> GND
- U4 pad 7: /CAN/CAN1_HI -> 3V3
- U4 pad 8: GND -> 3V3
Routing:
- net (no net): vias 2 -> 0
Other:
- board outline removed
